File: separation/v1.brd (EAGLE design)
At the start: 71.1 x 26.7 mm, 11 parts, among them IC1 L7805ACV

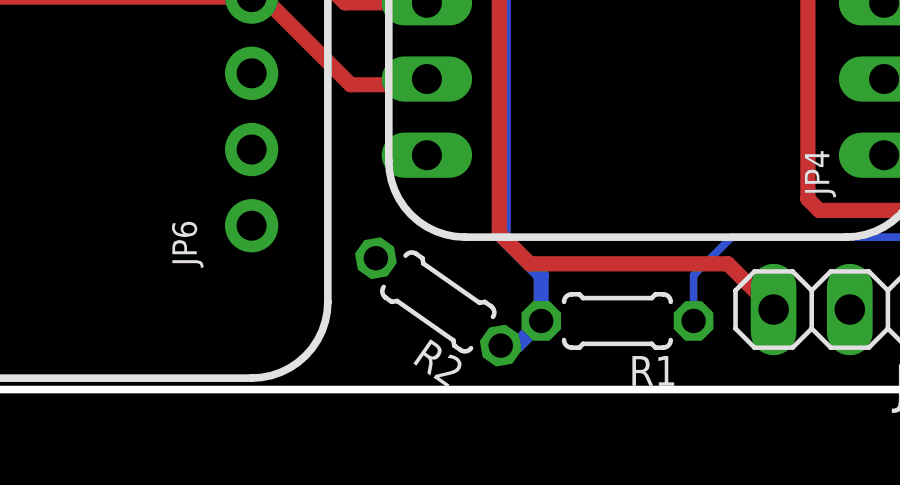
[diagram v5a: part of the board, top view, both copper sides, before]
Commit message: move r2 away from edge
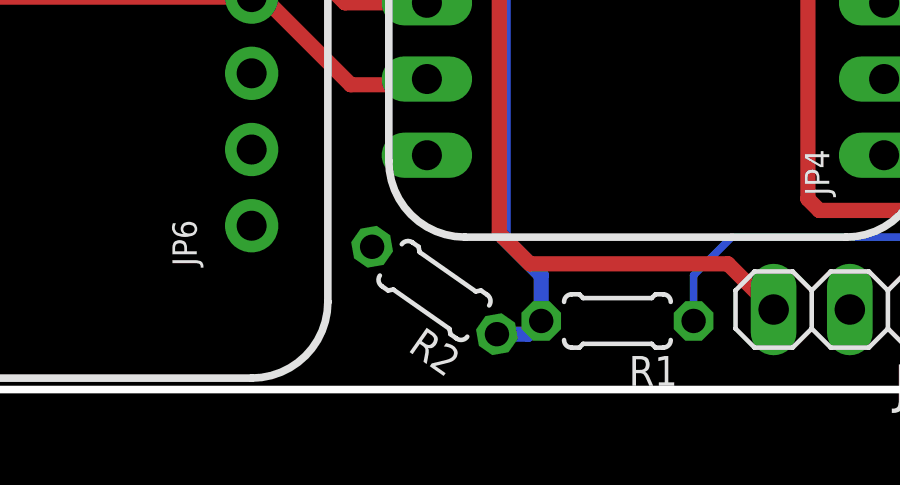
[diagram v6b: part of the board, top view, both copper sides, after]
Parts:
- moved R2 0.40 mm to (119.6, 55.4)
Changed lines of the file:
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@@
 <attribute name="VALUE" x="127.8636" y="56.6674" size="0.9906" layer="27" ratio="10" rot="R180"/>
 </element>
-<element name="R2" library="rcl" library_urn="urn:adsk.eagle:library:334" package="0204/5" package3d_urn="urn:adsk.eagle:package:23488/1" value="120k" x="119.761" y="54.991" smashed="yes" rot="R145">
-<attribute name="NAME" x="120.734540625" y="52.882953125" size="0.9906" layer="25" ratio="10" rot="R145"/>
-<attribute name="POPULARITY" value="35" x="119.761" y="54.991" size="1.778" layer="27" rot="R145" display="off"/>
-<attribute name="SPICEPREFIX" value="R" x="119.761" y="54.991" size="1.778" layer="27" rot="R145" display="off"/>
-<attribute name="VALUE" x="122.8345" y="55.66059375" size="0.9906" layer="27" ratio="10" rot="R145"/>
+<element name="R2" library="rcl" library_urn="urn:adsk.eagle:library:334" package="0204/5" package3d_urn="urn:adsk.eagle:package:23488/1" value="120k" x="119.634" y="55.372" smashed="yes" rot="R145">
+<attribute name="NAME" x="120.607540625" y="53.263953125" size="0.9906" layer="25" ratio="10" rot="R145"/>
+<attribute name="POPULARITY" value="35" x="119.634" y="55.372" size="1.778" layer="27" rot="R145" display="off"/>
+<attribute name="SPICEPREFIX" value="R" x="119.634" y="55.372" size="1.778" layer="27" rot="R145" display="off"/>
+<attribute name="VALUE" x="122.7075" y="56.04159375" size="0.9906" layer="27" ratio="10" rot="R145"/>
 </element>
 </elements>
@@
 <wire x1="147.51" y1="59.69" x2="140.97" y2="72.4" width="0" layer="19" extent="1-1"/>
 <wire x1="133.477" y1="54.737" x2="147.51" y2="59.69" width="0" layer="19" extent="1-1"/>
-<wire x1="117.680353125" y1="56.44788125" x2="133.477" y2="54.737" width="0" layer="19" extent="1-1"/>
-<wire x1="113.538" y1="62.611" x2="117.680353125" y2="56.44788125" width="0" layer="19" extent="1-1"/>
+<wire x1="117.553353125" y1="56.82888125" x2="133.477" y2="54.737" width="0" layer="19" extent="1-1"/>
+<wire x1="113.538" y1="62.611" x2="117.553353125" y2="56.82888125" width="0" layer="19" extent="1-1"/>
 <wire x1="113.538" y1="67.691" x2="113.538" y2="62.611" width="0" layer="19" extent="1-1"/>
 <wire x1="94.869" y1="62.738" x2="113.538" y2="62.611" width="0" layer="19" extent="1-1"/>
@@
 <wire x1="121.92" y1="71.12" x2="120.4595" y2="72.5805" width="0.508" layer="16"/>
 <wire x1="121.92" y1="57.15" x2="121.92" y2="71.12" width="0.508" layer="16"/>
-<wire x1="123.19" y1="54.356" x2="122.368115625" y2="53.534115625" width="0.508" layer="16"/>
-<wire x1="122.368115625" y1="53.534115625" x2="121.84164375" y2="53.534115625" width="0.508" layer="16"/>
+<wire x1="123.19" y1="54.356" x2="122.749115625" y2="53.915115625" width="0.508" layer="16"/>
+<wire x1="122.749115625" y1="53.915115625" x2="121.71464375" y2="53.915115625" width="0.508" layer="16"/>
 </signal>
 </signals>
